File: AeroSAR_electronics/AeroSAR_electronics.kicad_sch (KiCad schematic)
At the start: 0 parts

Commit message: Added the Wifi module to the schematic and started working on fc-top
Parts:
- added J1: USB_A, symbol Connector:USB_A
- added WiFi_module: ~, BL-M8812EU2:BL-M8812EU2, symbol WiFi_module:BL-M8812EU2
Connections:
- new net: J1.2 (D-), WiFi_module.3 (DM)
- new net: J1.3 (D+), WiFi_module.2 (DP)
- new net: J1.4 (GND), WiFi_module.18 (GND)
- no-connect marks 0 -> 17

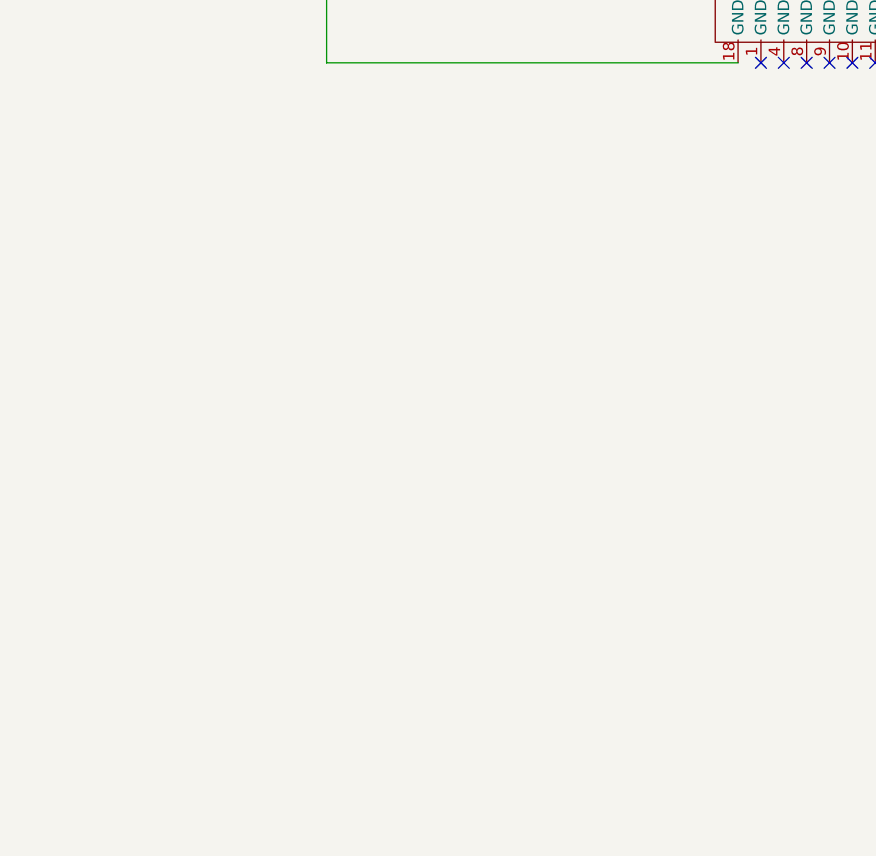
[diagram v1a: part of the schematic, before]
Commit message: Rearranged the FC-top schematic pins & created a basic pcb outline
Edited the pin type for most of the ground pins
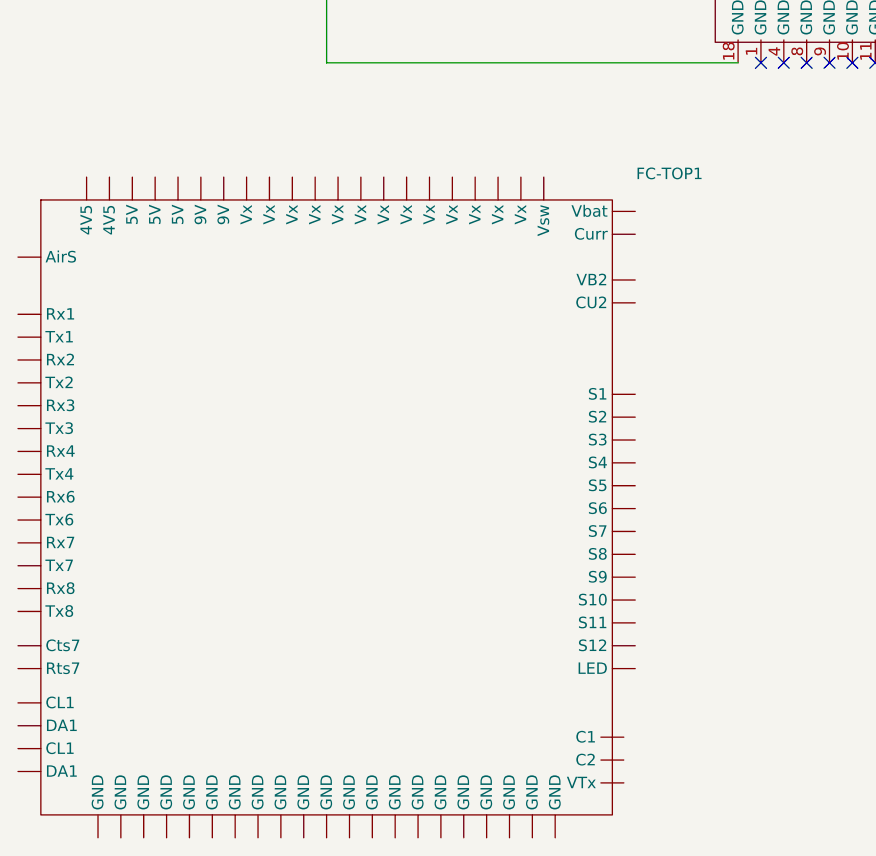
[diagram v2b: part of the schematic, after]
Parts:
- added FC-TOP1: ~, symbol Flight_Controller:top
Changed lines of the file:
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@@
+		)
+	)
+	(symbol
+		(lib_id "Flight_Controller:top")
+		(at 50.8 104.14 0)
+		(unit 1)
+		(exclude_from_sim no)
+		(in_bom yes)
+		(on_board yes)
+		(dnp no)
+		(fields_autoplaced yes)
+		(property "Reference" "FC-TOP1"
+			(at 143.51 101.2346 0)
+			(effects
+				(font
+					(size 1.27 1.27)
+				)
+			)
+		)
+		(property "Value" "~"
+			(at 143.51 103.1397 0)
+			(effects
+				(font
+					(size 1.27 1.27)
+				)
+			)
+		)
+		(property "Footprint" ""
+			(at 50.8 104.14 0)
+			(effects
+				(font
+					(size 1.27 1.27)
+				)
+				(hide yes)
+			)
+		)
+		(property "Datasheet" ""
+			(at 50.8 104.14 0)
+			(effects
+				(font
+					(size 1.27 1.27)
+				)
+				(hide yes)
+			)
+		)
+		(property "Description" ""
+			(at 50.8 104.14 0)
+			(effects
+				(font
+					(size 1.27 1.27)
+				)
+				(hide yes)
+			)
+		)
+		(pin ""
+		)
+		(pin ""
+		)
+		(pin ""
+		)
+		(pin ""
+		)
+		(pin ""
+		)
+		(pin ""
+		)
+		(pin ""
+		)
+		(pin ""
+		)
+		(pin ""
+		)
+		(pin ""
+		)
+		(pin ""
+		)
+		(pin ""
+		)
+		(pin ""
+		)
+		(pin ""
+		)
+		(pin ""
+		)
+		(pin ""
+		)
+		(pin ""
+		)
+		(pin ""
+		)
+		(pin ""
+		)
+		(pin ""
+		)
+		(pin ""
+		)
+		(pin ""
+		)
+		(pin ""
+		)
+		(pin ""
+		)
+		(pin ""
+		)
+		(pin ""
+		)
+		(pin ""
+		)
+		(pin ""
+		)
+		(pin ""
+		)
+		(pin ""
+		)
+		(pin ""
+		)
+		(pin ""
+		)
+		(pin ""
+		)
+		(pin ""
+		)
+		(pin ""
+		)
+		(pin ""
+		)
+		(pin ""
+		)
+		(pin ""
+		)
+		(pin ""
+		)
+		(pin ""
+		)
+		(pin ""
+		)
+		(pin ""
+		)
+		(pin ""
+		)
+		(pin ""
+		)
+		(pin ""
+		)
+		(pin ""
+		)
+		(pin ""
+		)
+		(pin ""
+		)
+		(pin ""
+		)
+		(pin ""
+		)
+		(pin ""
+		)
+		(pin ""
+		)
+		(pin ""
+		)
+		(pin ""
+		)
+		(pin ""
+		)
+		(pin ""
+		)
+		(pin ""
+		)
+		(pin ""
+		)
+		(pin ""
+		)
+		(pin ""
+		)
+		(pin ""
+		)
+		(pin ""
+		)
+		(pin ""
+		)
+		(pin ""
+		)
+		(pin ""
+		)
+		(pin ""
+		)
+		(pin ""
+		)
+		(pin ""
+		)
+		(pin ""
+		)
+		(pin ""
+		)
+		(pin ""
+		)
+		(pin ""
+		)
+		(pin ""
+		)
+		(pin ""
+		)
+		(pin ""
+		)
+		(pin ""
+		)
+		(pin ""
+		)
+		(pin ""
+		)
+		(pin ""
+		)
+		(pin ""
+		)
+		(pin ""
+		)
+		(pin ""
+		)
+		(pin ""
+		)
+		(instances
+			(project ""
+				(path "/da961784-12b1-4f58-8e7d-3aa55c43f0e3"
+					(reference "FC-TOP1")
+					(unit 1)
+				)
+			)
 		)
 	)

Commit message: Prepared v1 of the schematic
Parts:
- removed WiFi_module: ~, BL-M8812EU2:BL-M8812EU2, symbol WiFi_module:BL-M8812EU2
- added C1: C, Capacitor_SMD:C_0805_2012Metric, symbol Device:C
- added J10: Receiver, symbol Connector:Conn_01x01_Pin
- added J11: Rpi, symbol Connector:Conn_01x02_Pin
- added J12: GPS, symbol Connector:Conn_01x02_Pin
- added J2: ESC-1, symbol Connector:Conn_01x03_Pin
- added J3: ESC-2, symbol Connector:Conn_01x03_Pin
- added J4, J5, J6, J7, J8: Servo, symbol Connector:Conn_01x03_Pin
- added J9: Compass, symbol Connector:Conn_01x02_Pin
- added WiFi_module1: ~, H743-WING-Top, symbol WiFi_module:BL-M8812EU2
- FC-TOP1: footprint (none) -> H743-WING-Top
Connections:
- net at J1.2 (D-): now also WiFi_module1.3 (DM)
- net at J1.3 (D+): now also WiFi_module1.2 (DP)
- net GND: now reaches J1.4 (GND)
- net GND: now also FC-TOP1.21 (GND), C1.2, WiFi_module1.1 (GND), WiFi_module1.10 (GND), WiFi_module1.11 (GND), WiFi_module1.12 (GND), WiFi_module1.13 (GND), WiFi_module1.14 (GND), WiFi_module1.15 (GND), WiFi_module1.16 (GND), WiFi_module1.17 (GND), WiFi_module1.18 (GND), WiFi_module1.4 (GND), WiFi_module1.8 (GND), WiFi_module1.9 (GND)
- new net: FC-TOP1.79 (Rx4), J10.1 (Pin_1)
- new net: FC-TOP1.18 (GND), J6.1 (Pin_1)
- new net: FC-TOP1.27 (Vx), J6.2 (Pin_2)
- new net: FC-TOP1.36 (S5), J6.3 (Pin_3)
- new net: FC-TOP1.14 (GND), J2.1 (Pin_1)
- new net: FC-TOP1.12 (S1), J2.3 (Pin_3)
- new net: FC-TOP1.15 (GND), J3.1 (Pin_1)
- new net: FC-TOP1.33 (S2), J3.3 (Pin_3)
- new net: FC-TOP1.67 (Rx2), J12.1 (Pin_1)
- new net: FC-TOP1.66 (Tx2), J12.2 (Pin_2)
- new net: FC-TOP1.65 (CL1), J9.1 (Pin_1)
- new net: FC-TOP1.64 (DA1), J9.2 (Pin_2)
- new net: FC-TOP1.77 (Rx3), J11.1 (Pin_1)
- new net: FC-TOP1.76 (Tx3), J11.2 (Pin_2)
- new net: FC-TOP1.20 (GND), J8.1 (Pin_1)
- new net: FC-TOP1.29 (Vx), J8.2 (Pin_2)
- new net: FC-TOP1.38 (S7), J8.3 (Pin_3)
- new net: FC-TOP1.19 (GND), J7.1 (Pin_1)
- new net: FC-TOP1.28 (Vx), J7.2 (Pin_2)
- new net: FC-TOP1.37 (S6), J7.3 (Pin_3)
- new net: FC-TOP1.17 (GND), J5.1 (Pin_1)
- new net: FC-TOP1.26 (Vx), J5.2 (Pin_2)
- new net: FC-TOP1.35 (S4), J5.3 (Pin_3)
- new net: FC-TOP1.16 (GND), J4.1 (Pin_1)
- new net: FC-TOP1.25 (Vx), J4.2 (Pin_2)
- new net: FC-TOP1.34 (S3), J4.3 (Pin_3)
- new net GND-GPS&Compass: FC-TOP1.83 (GND)
- new net GND-PDB: FC-TOP1.10 (GND)
- new net GND-Receiver: FC-TOP1.23 (GND)
- new net VCC: C1.1, WiFi_module1.6 (VDD5)
- new net VCC-GPS&Compass: FC-TOP1.82 (4V5)
- new net VCC-PDB: FC-TOP1.11 (Vx)
- new net VCC-Receiver: FC-TOP1.32 (Vx)
- new net VCC-WiFi: FC-TOP1.30 (Vx)
- no-connect marks 17 -> 55
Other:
- moved on the sheet: J1

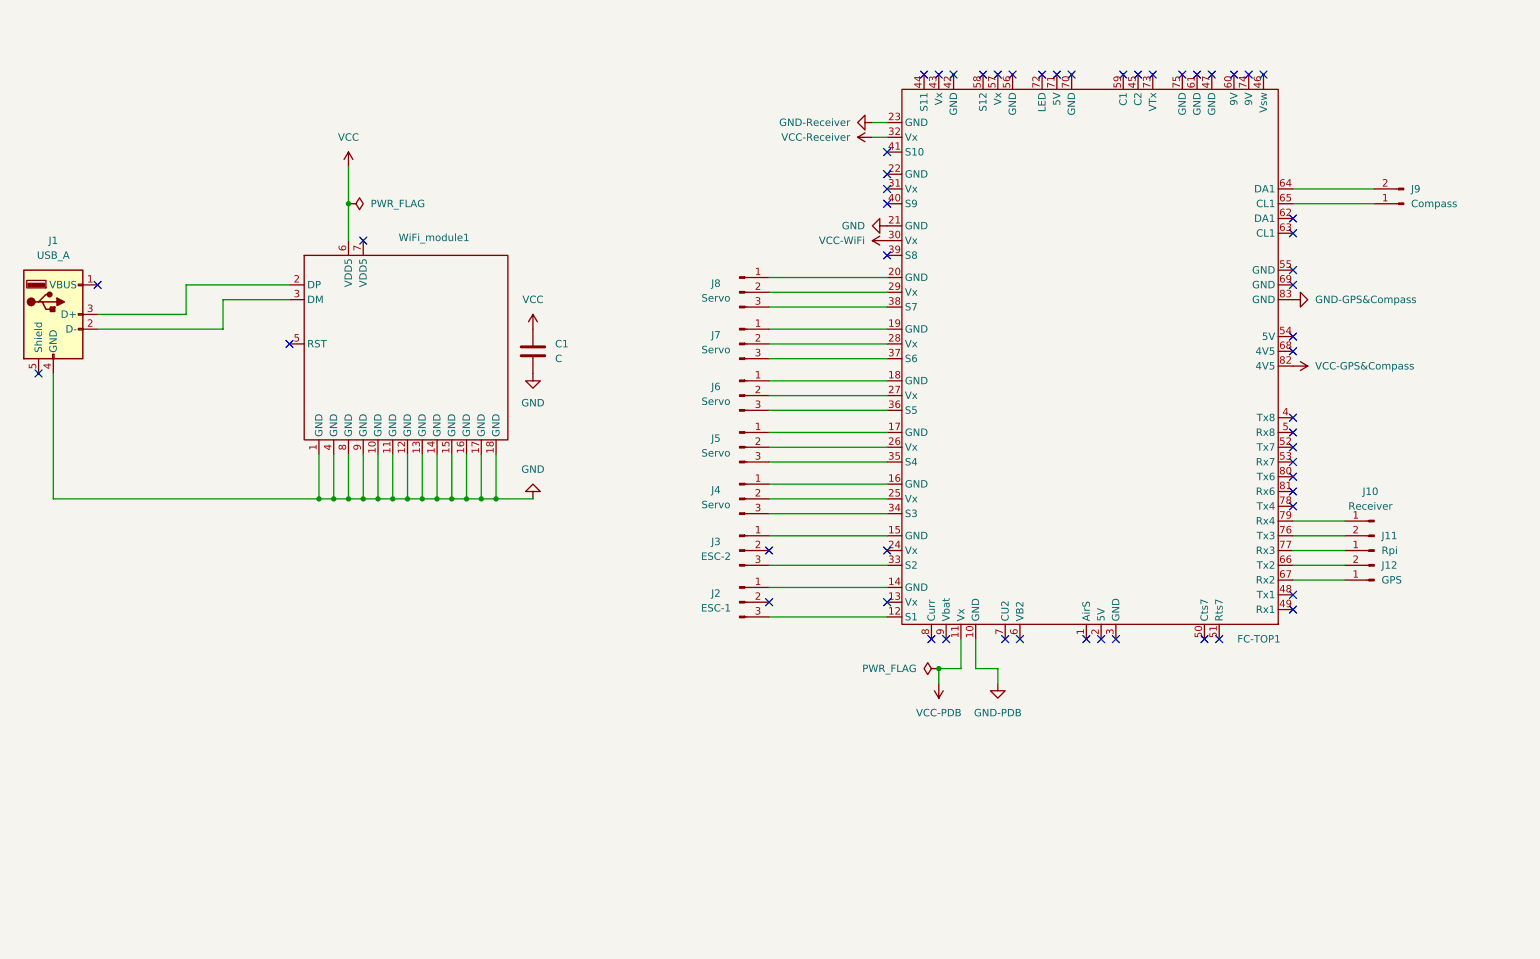
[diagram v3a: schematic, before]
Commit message: Fixed footprint not loading on schematic and replaced the usb A with usb micro
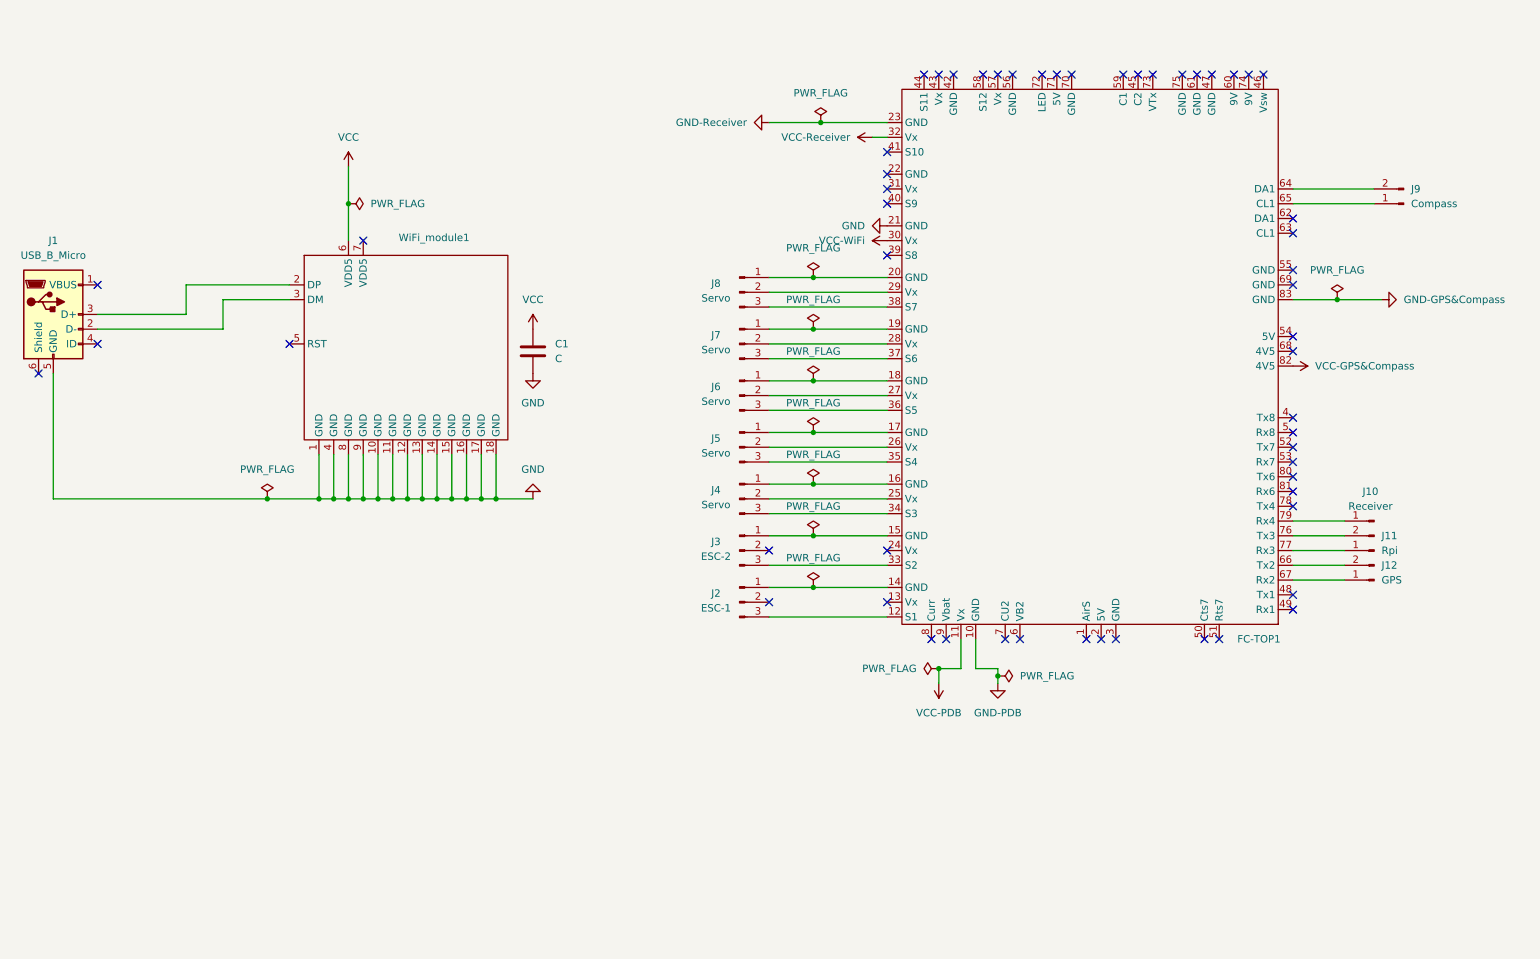
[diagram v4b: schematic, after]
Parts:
- removed J1: USB_A, symbol Connector:USB_A
- added J1: USB_B_Micro, Connector_USB:USB_Micro-B_Amphenol_10103594-0001LF_Horizontal, symbol Connector:USB_B_Micro
- FC-TOP1: footprint H743-WING-Top -> Flight_Controller_Top:H743-WING_TOP
- WiFi_module1: footprint H743-WING-Top -> BL-M8812EU2:BL-M8812EU2
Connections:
- net GND: now also J1.5 (GND)
- net at WiFi_module1.3 (DM): now also J1.2 (D-)
- net at WiFi_module1.2 (DP): now also J1.3 (D+)
- no-connect marks 55 -> 56

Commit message: Added usb and power to the PCB
Edited the FC footprint for mounting as well
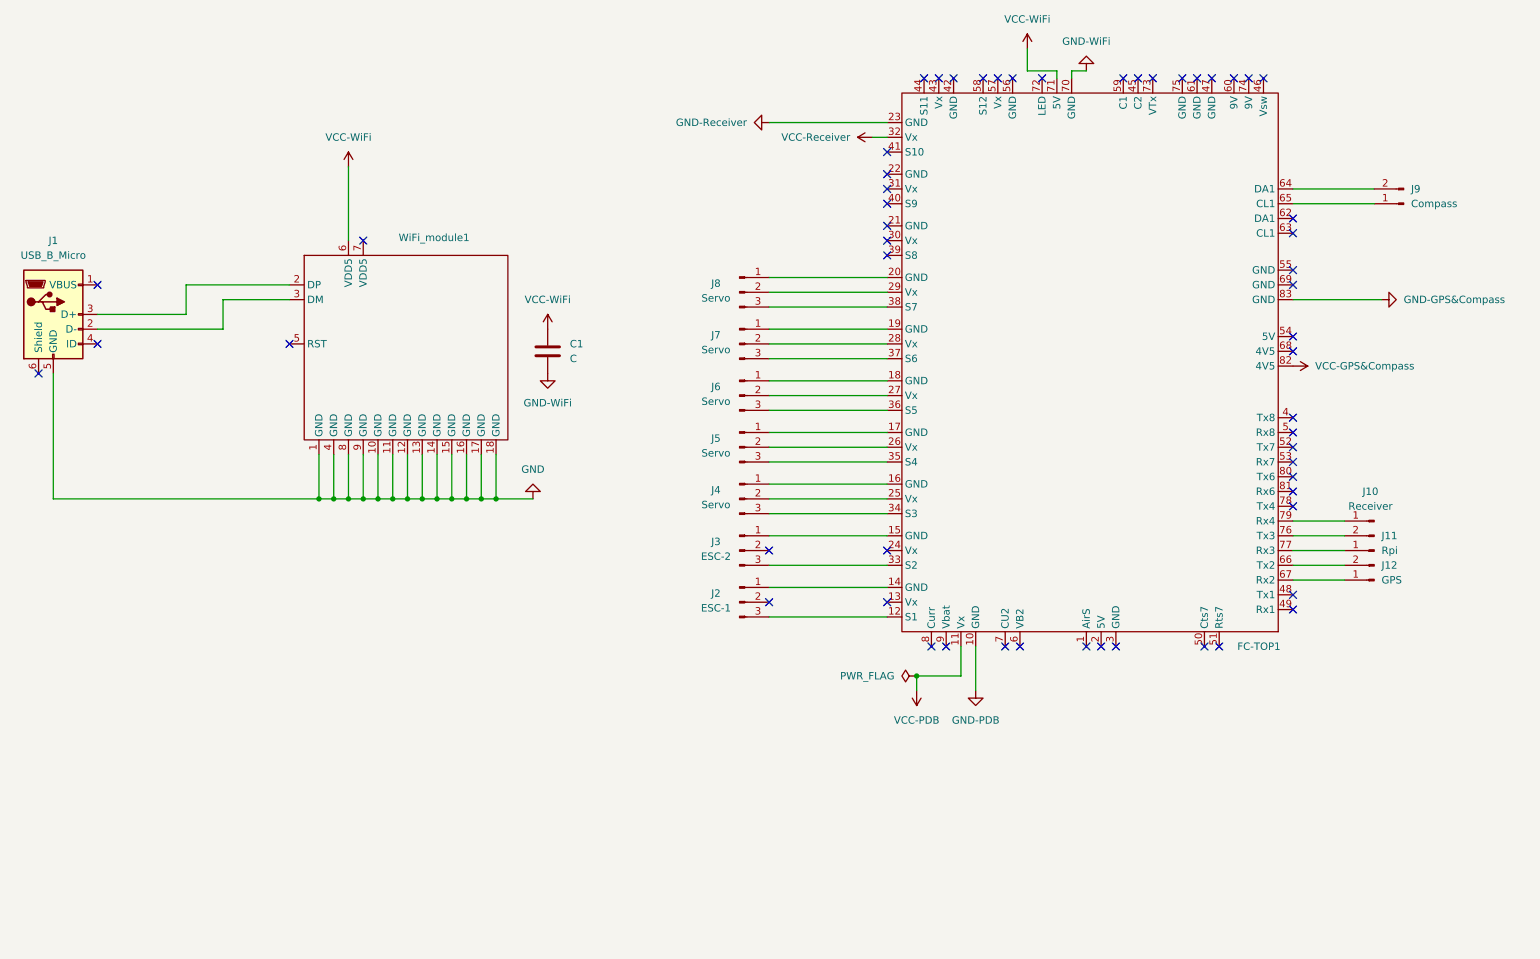
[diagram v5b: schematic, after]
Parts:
- J1: footprint Connector_USB:USB_Micro-B_Amphenol_10103594-0001LF_Horizontal -> Connector_USB:USB_Micro-B_Wuerth_614105150721_Vertical
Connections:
- net VCC is gone; now on net VCC-WiFi: C1.1, WiFi_module1.6 (VDD5)
- net GND: no longer C1.2, FC-TOP1.21 (GND)
- net VCC-WiFi: now also FC-TOP1.71 (5V); no longer FC-TOP1.30 (Vx)
- net GND-WiFi: now reaches FC-TOP1.70 (GND)
- net GND-WiFi: now also C1.2
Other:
- moved on the sheet: C1
